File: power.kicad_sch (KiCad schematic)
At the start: 70 parts, among them J2 Molex_Mini-Fit_2x3_50362462, Q16 DMG1012T-7, Q2 SISS05DN-T1-GE3, Q23 SISS05DN-T1-GE3, Q24 SISS05DN-T1-GE3, Q25 SISS05DN-T1-GE3, Q5 SISS05DN-T1-GE3, Q6 DMG1012T-7, Q9 SISS05DN-T1-GE3, U15 NCP730BMT330_WSON, U6 LTC4412IS6, U61 LTC4412IS6, U62 LTC4412IS6, U63 LTC4412IS6, U64 LTC4412IS6

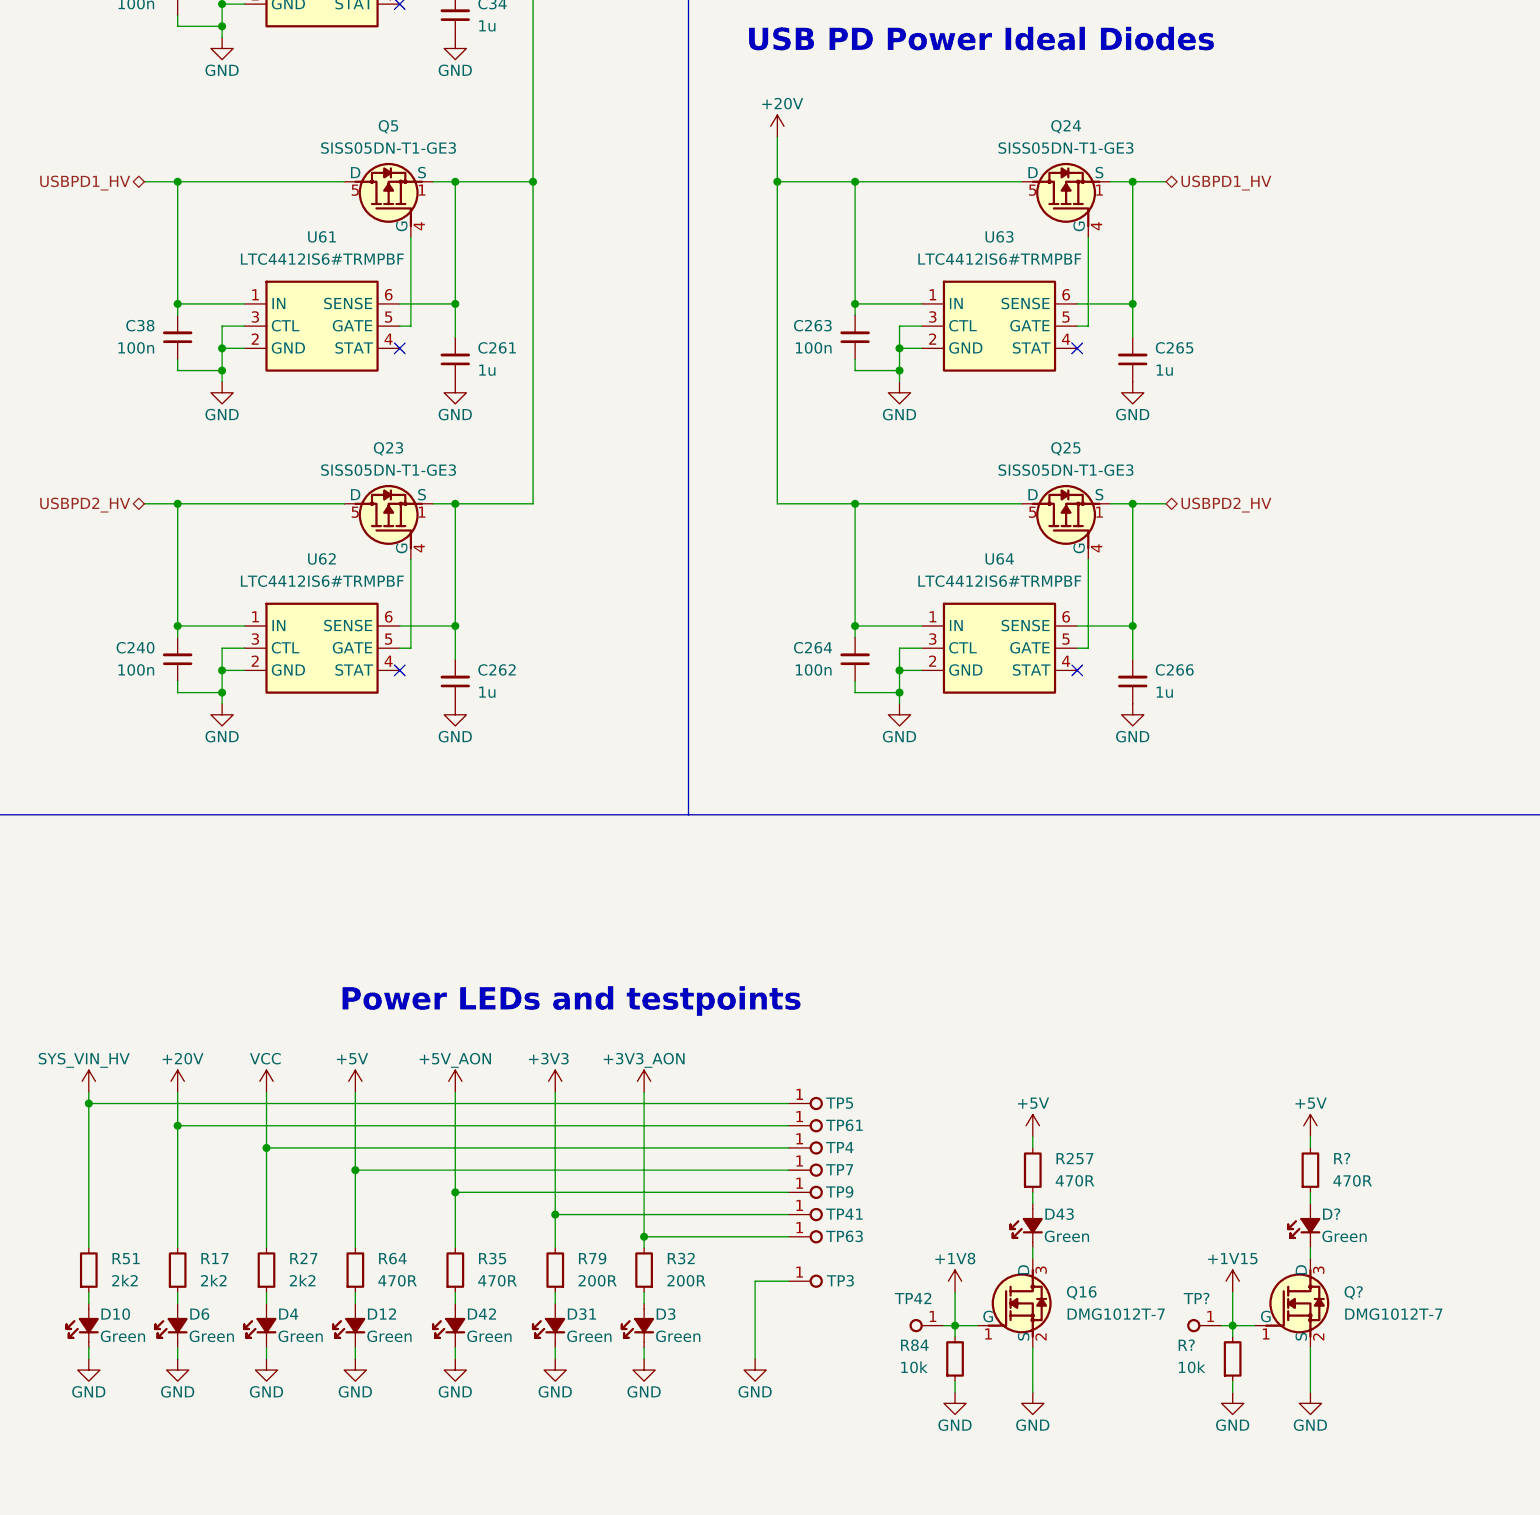
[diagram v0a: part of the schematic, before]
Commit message: [#85326] Fix annotation, set USBPD ideal diodes to DNP, add DC-DC rule zones
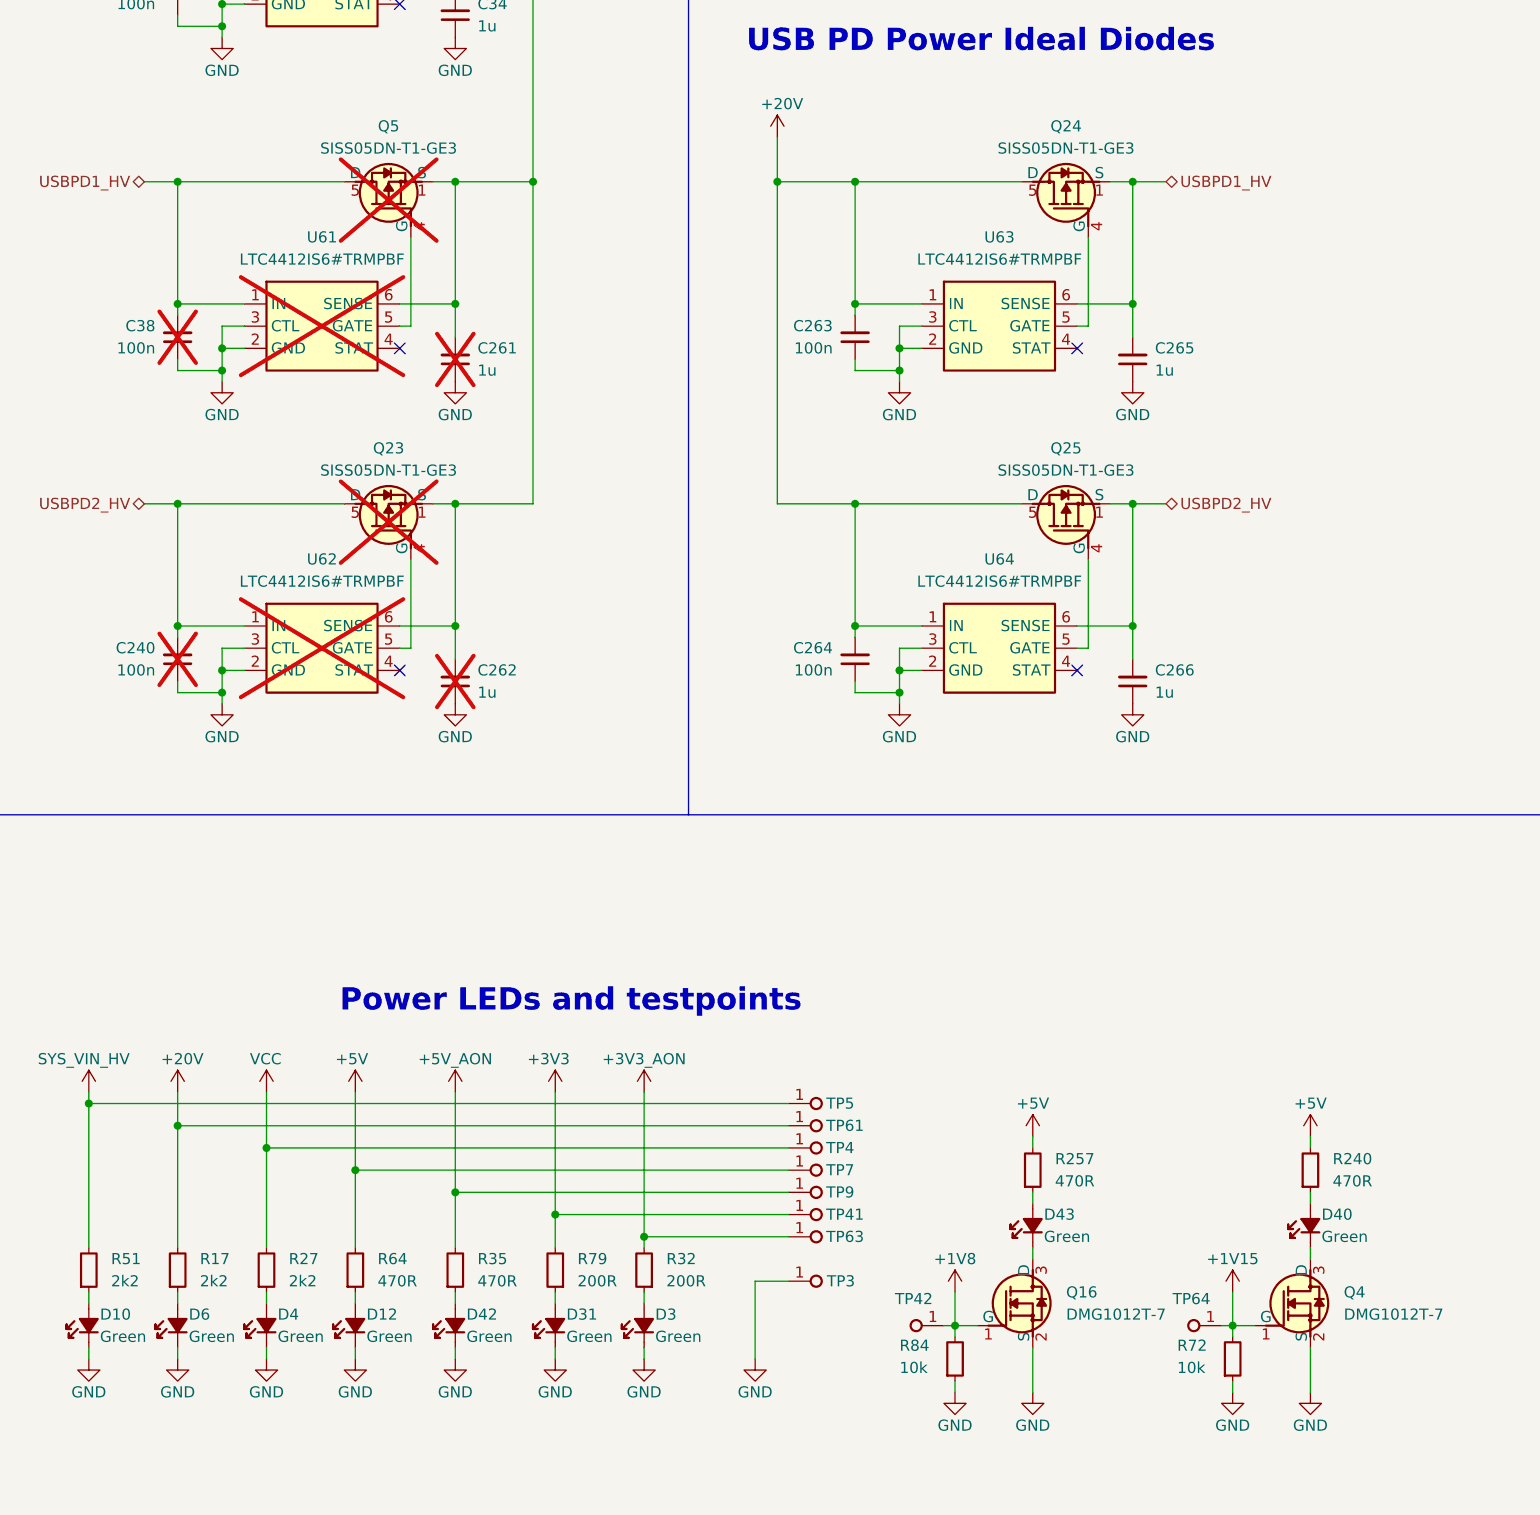
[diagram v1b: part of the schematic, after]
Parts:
- removed D?: LED_G_0603_LTST-C190GKT, antmicro-footprints:LED_0603_1608Metric_G, symbol antmicroLEDIndicationDiscrete:LED_G_0603_LTST-C190GKT
- removed Q?: DMG1012T-7, antmicro-footprints:SOT-523, symbol antmicroTransistorsFETsMOSFETsSingle:DMG1012T-7
- removed R?: R_10k_0402, antmicro-footprints:R_0402_1005Metric, symbol antmicroResistors0402:R_10k_0402
- removed R?: R_470R_0402, antmicro-footprints:R_0402_1005Metric, symbol antmicroResistors0402:R_470R_0402
- removed TP?: TP_0.75mm_SMD, antmicro-footprints:TP_SMD_0.75mm, symbol antmicroTestPoints:TP_0.75mm_SMD
- added D40: LED_G_0603_LTST-C190GKT, antmicro-footprints:LED_0603_1608Metric_G, symbol antmicroLEDIndicationDiscrete:LED_G_0603_LTST-C190GKT
- added Q4: DMG1012T-7, antmicro-footprints:SOT-523, symbol antmicroTransistorsFETsMOSFETsSingle:DMG1012T-7
- added R240: R_470R_0402, antmicro-footprints:R_0402_1005Metric, symbol antmicroResistors0402:R_470R_0402
- added R72: R_10k_0402, antmicro-footprints:R_0402_1005Metric, symbol antmicroResistors0402:R_10k_0402
- added TP64: TP_0.75mm_SMD, antmicro-footprints:TP_SMD_0.75mm, symbol antmicroTestPoints:TP_0.75mm_SMD
- C240, C261, C262, C38, U61, U62: now not fitted; now left out of the parts list
- Q23, Q5: now not fitted
- Q24, Q25: now in the parts list
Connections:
- net +1V15: now also Q4.1 (G), R72.2, TP64.1
- net +5V: now also R240.2
- net GND: now also Q4.2 (S), R72.1
- new net: D40.1 (C), Q4.3 (D)
- new net: D40.2 (A), R240.1

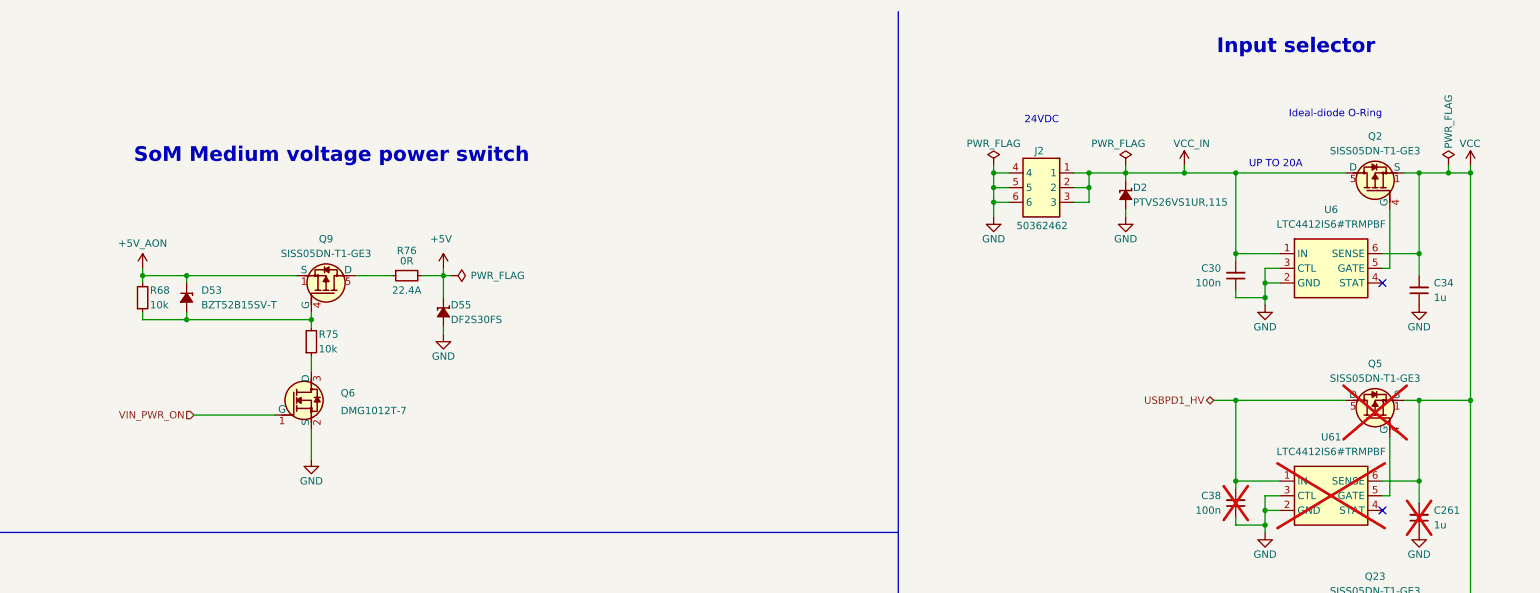
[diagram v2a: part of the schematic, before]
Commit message: [#85488] Power sections improvements
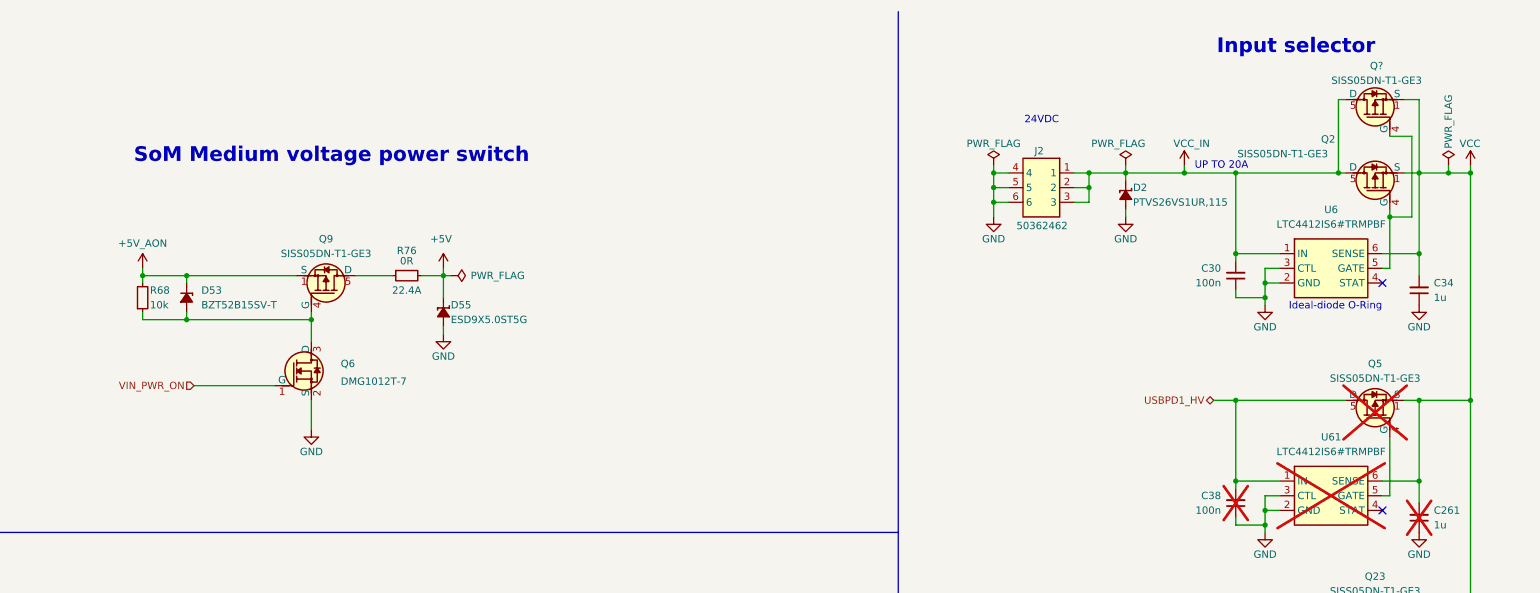
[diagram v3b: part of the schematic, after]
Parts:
- removed R75: R_10k_0402, antmicro-footprints:R_0402_1005Metric, symbol antmicroResistors0402:R_10k_0402
- added Q?: SISS05DN-T1-GE3, antmicro-footprints:Vishay_PowerPAK_1212-8_Single, symbol antmicroTransistorsFETsMOSFETsSingle:SISS05DN-T1-GE3
- D55: value DF2S30FS_SOD -> ESD9X5.0ST5G; symbol antmicroTVSDiodes:DF2S30FS_SOD -> antmicroTVSDiodes:ESD9X5.0ST5G; MPN DF2S30FS -> ESD9X5.0ST5G; Manufacturer Toshiba -> ON Semiconductor
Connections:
- net VCC: now also Q?.1 (S), Q?.2 (S), Q?.3 (S)
- net VCC_IN: now also Q?.5 (D)
- net at Q2.4 (G), U6.5 (GATE): now also Q?.4 (G)
- net at D53.2 (A), Q9.4 (G), R68.1: now also Q6.3 (D)
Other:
- moved on the sheet: Q6
